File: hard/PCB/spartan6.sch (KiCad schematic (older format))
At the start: 25 parts, among them IC1 W9812G6KH, P1 CONN_02X20, U1 XC6SLX9-2TQG144C

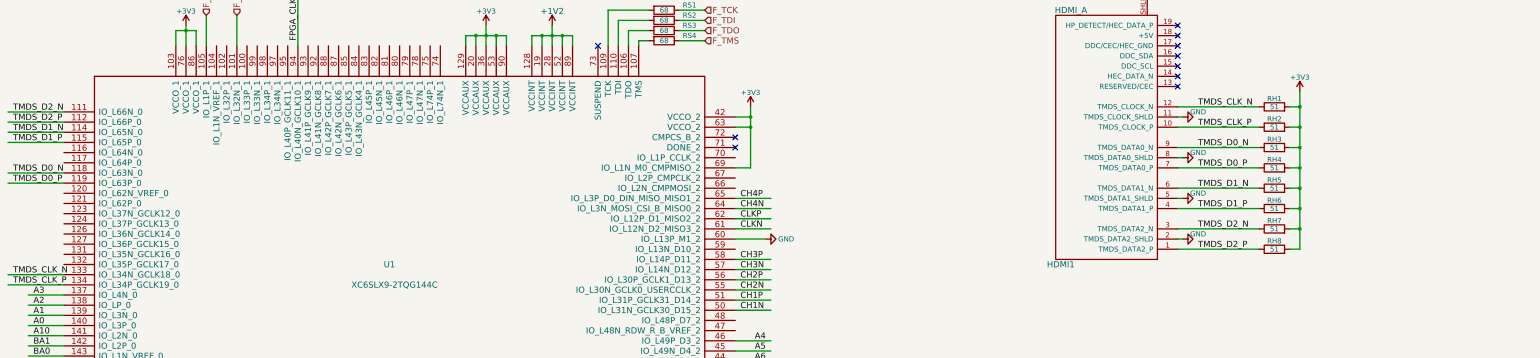
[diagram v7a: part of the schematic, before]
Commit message: se modifican el pin hdmi- las resitencias RN1 - eñ conector de  voltaje
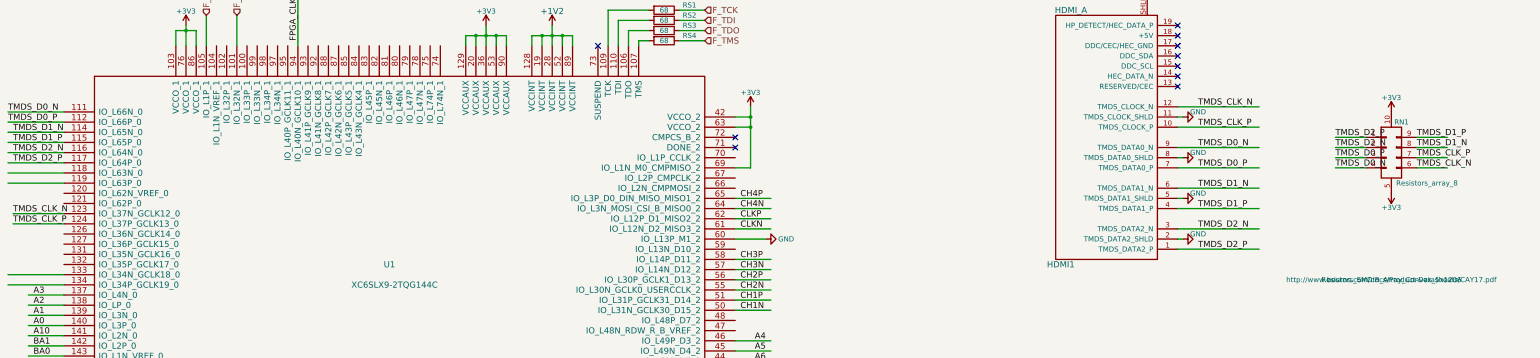
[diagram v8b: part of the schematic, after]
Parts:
- removed RH1, RH2, RH3, RH4, RH5, RH6, RH7, RH8: 51, Resistors_SMD:R_0402, symbol R
- added RN1: Resistors_array_8, Resistors_SMD:R_Array_Convex_5x1206, symbol Resistors_array_8
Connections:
- wire segments 295 -> 298
